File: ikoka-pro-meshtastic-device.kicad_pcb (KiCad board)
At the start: 2 copper layers, 80 x 100 mm, 63 parts, among them J1 Barrel_Jack_Switch, J10 BWSMA-KWE-Z001, J2 Conn_ARM_JTAG_SWD_10, J3 BWSMA-KWE-Z001, J4 Conn_01x01, J5 Conn_01x01, J6 Conn_01x01, J7 Conn_01x01, J8 USB_C_Receptacle_USB2.0_16P, SW2 TS36CA-0.6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

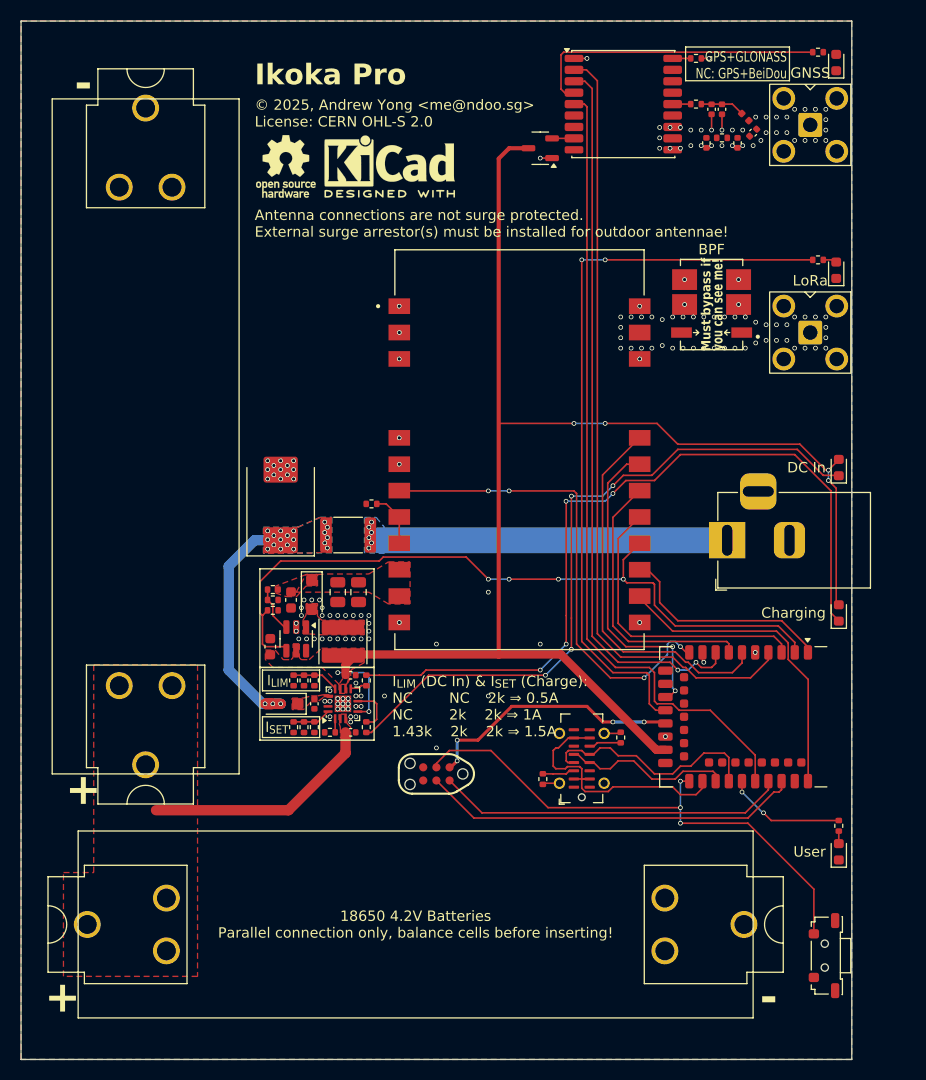
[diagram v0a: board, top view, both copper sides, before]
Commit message: feat: I2C and 100k+300k VBAT divider
Fixes #1

Signed-off-by: Andrew Yong <me@ndoo.sg>
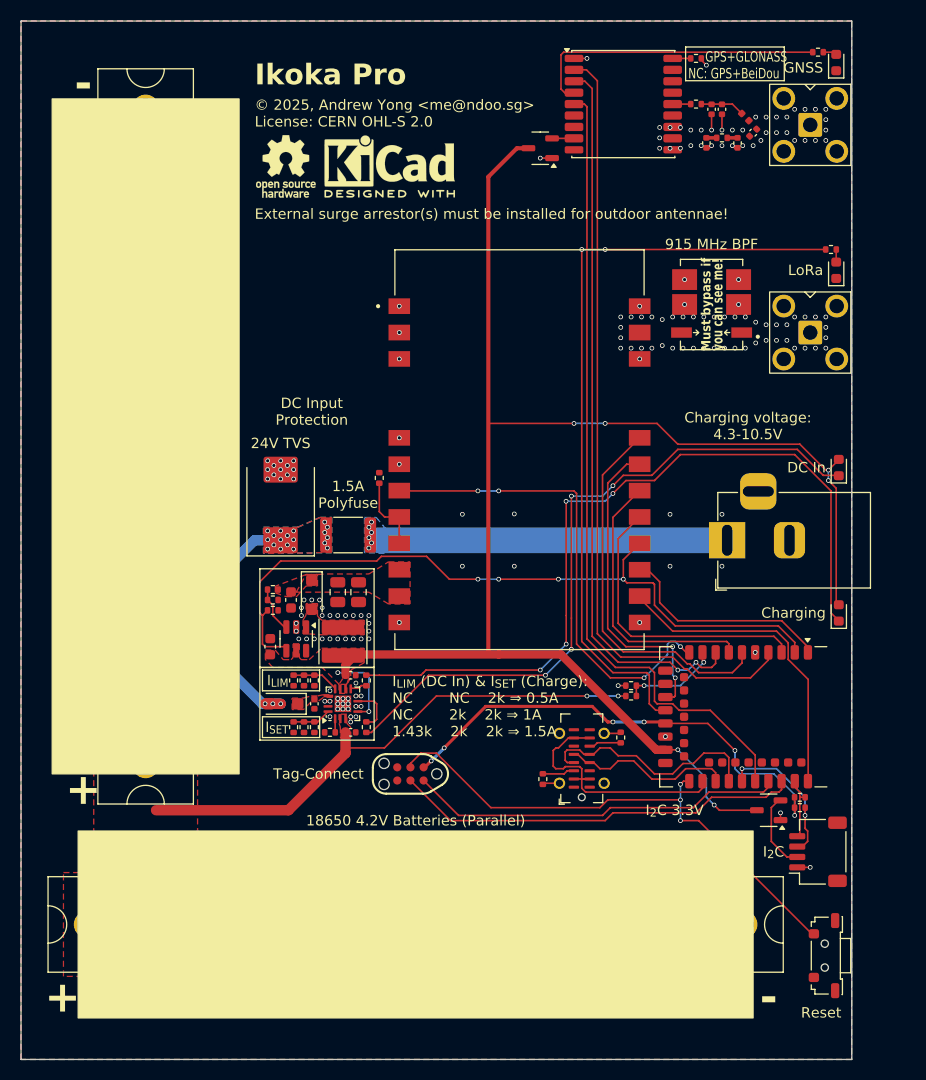
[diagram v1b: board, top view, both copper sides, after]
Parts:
- removed D6: LED, LED_SMD:LED_0603_1608Metric
- removed R16: 470, Resistor_SMD:R_0402_1005Metric
- added J9: SM04B-SRSS-TB, Connector_JST:JST_SH_SM04B-SRSS-TB_1x04-1MP_P1.00mm_Horizontal, F.Cu at (186.8, 130.0)
- added R22: 300k, Resistor_SMD:R_0402_1005Metric, F.Cu at (168.8, 115.0)
- added R23: 100k, Resistor_SMD:R_0402_1005Metric, F.Cu at (168.8, 114.0)
- added R24: 4.7k, Resistor_SMD:R_0402_1005Metric, F.Cu at (185.0, 124.8)
- added R25: 4.7k, Resistor_SMD:R_0402_1005Metric, F.Cu at (185.0, 125.8)
- added U7: XC6206P332MR, Package_TO_SOT_SMD:SOT-23-3, F.Cu at (182.0, 126.0)
- moved R11 2.61 mm to (144.5, 94.0), turned to 90 degrees
- moved J2 2.50 mm to (147.5, 122.5)
- moved R15 1.60 mm to (188.0, 72.0)
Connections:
- net /CHG_LED renamed /Power/CHG_LED
- net /PGOOD_LED renamed /Power/PGOOD_LED
- net LED_PPS renamed Net-(U3-TIMEPULSE)
- U5 pad 33: LED_USER -> I2C_SDA
- U5 pad 41: unconnected-(U5-P0.09/NFC1-Pad41) -> I2C_SCL
- U5 pad 9: VBAT_SENSE -> BATTERY_PIN
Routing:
- net V_{BAT}: track 22.5 -> 51.6 mm, vias 0 -> 2
- net V_{DD}_NRF: track 25.1 -> 46.5 mm, vias 4 -> 6
- net I2C_SDA: track 0.00 -> 14.7 mm, vias 0 -> 2
- net V_{SYS}: track 143.0 -> 156.2 mm, vias 6 -> 8
- net LED_USER: track 11.5 -> 0.00 mm, vias 2 -> 0
- net BATTERY_PIN: track 0.00 -> 9.44 mm, vias 0 -> 2
- net Net-(J9-Pin_2): track 0.00 -> 7.43 mm
- net I2C_SCL: track 0.00 -> 6.07 mm
- net GND: track 11.2 -> 14.0 mm, vias 169 -> 174
- net SWCLK: track 36.7 -> 39.4 mm
- net SWDIO: track 33.7 -> 36.3 mm
- net LED_PIN: track 71.4 -> 73.6 mm
- net LORA_TXEN: track 5.23 -> 7.42 mm
- net Net-(D7-A): track 0.00 -> 1.33 mm
- net Net-(D6-A): track 1.22 -> 0.00 mm
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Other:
- board text added: "1.5A Polyfuse"
- board text added: "18650 4.2V Batteries (Parallel)"
- board text added: "24V TVS"
- board text added: "915 MHz BPF"
- board text added: "Charging voltage: 4.3-10.5V"
- board text added: "DC Input Protection"
- board text added: "External surge arrestor(s) must be installed for outdoor antennae!"
- board text added: "I_{2}C"
- board text added: "I_{2}C 3.3V"
- board text added: "Reset"
- board text added: "Tag-Connect"
- board text removed: "18650 4.2V Batteries Parallel connection only, balance cells before inserting!"
- board text removed: "Antenna connections are not surge protected. External surge arrestor(s) must be installed for outdoor antennae!"
- board text removed: "BPF"
- board text removed: "User"

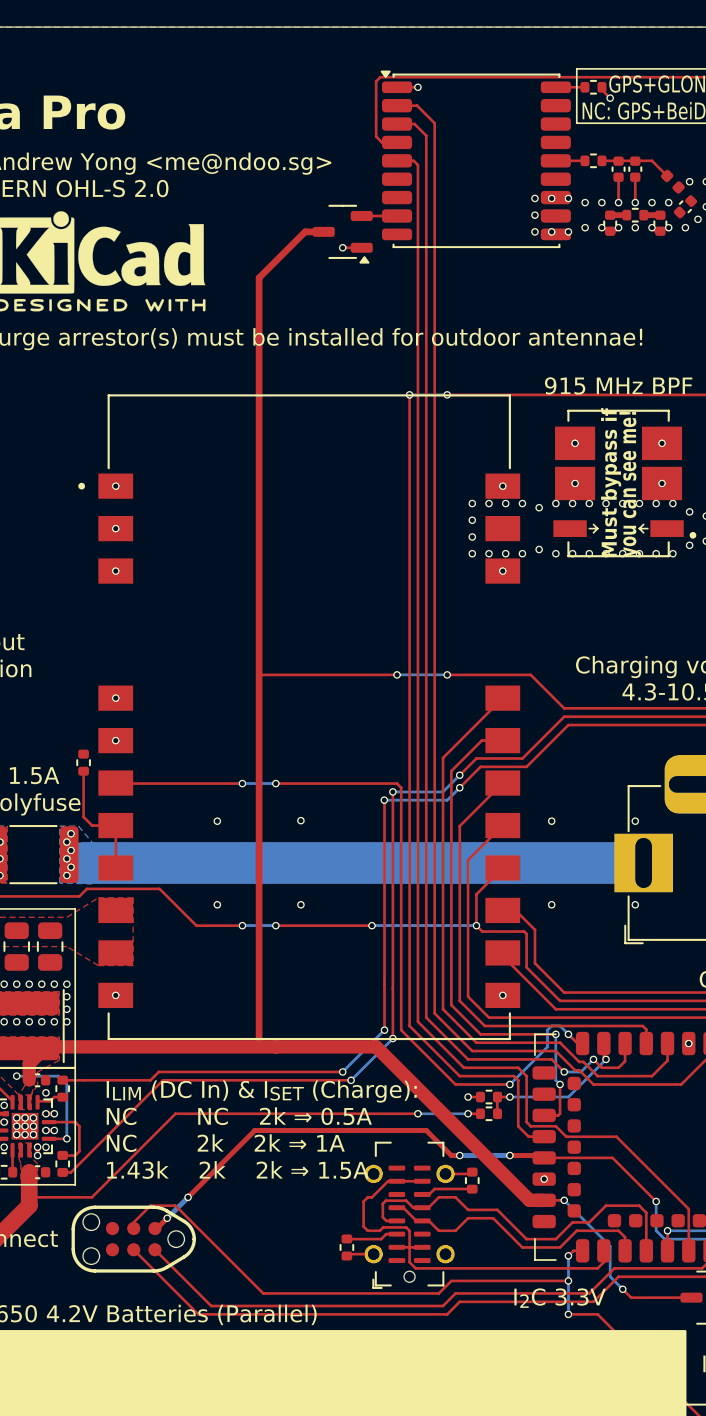
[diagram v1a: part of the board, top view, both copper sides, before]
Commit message: chore: v0.9.0 and JLCPCB order placeholder silkscreen
Signed-off-by: Andrew Yong <me@ndoo.sg>
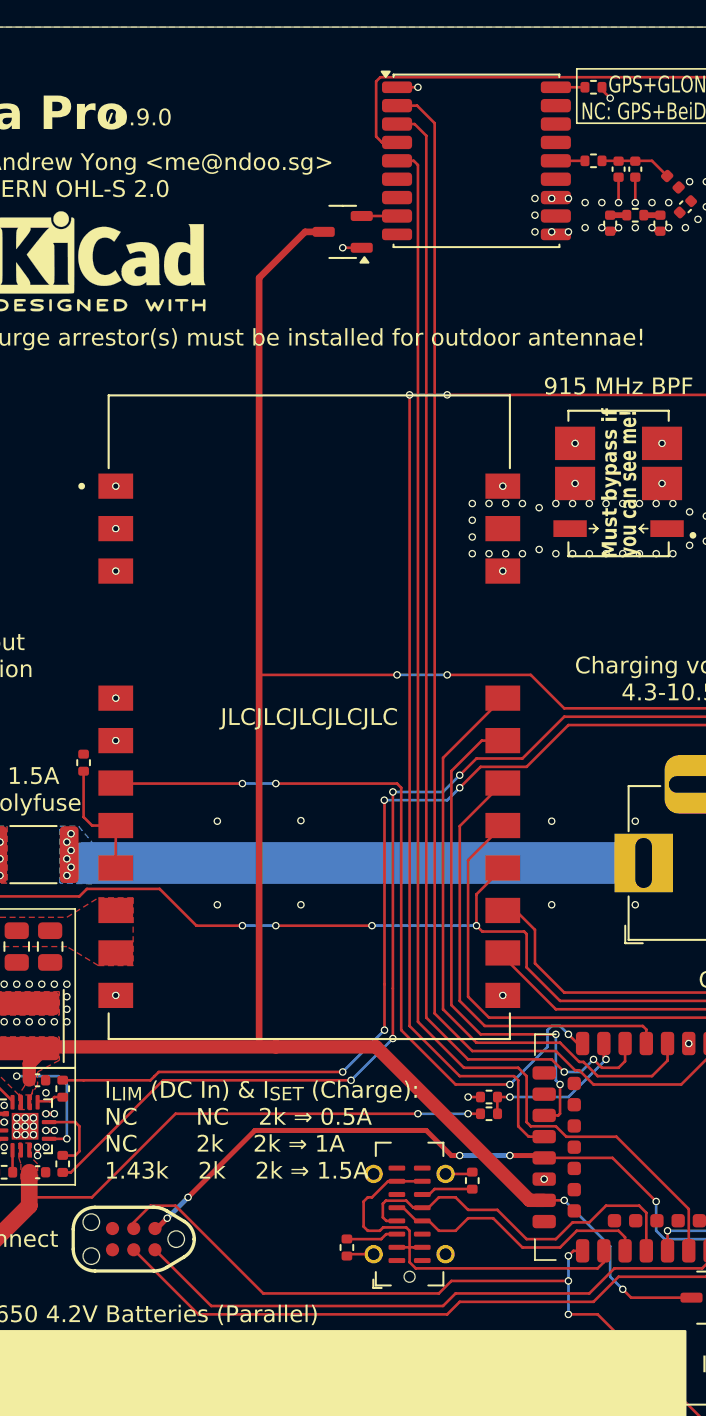
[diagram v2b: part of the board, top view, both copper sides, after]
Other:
- board text added: "JLCJLCJLCJLCJLC"
- board text added: "v0.9.0"
- board text removed: "I_{2}C 3.3V"
